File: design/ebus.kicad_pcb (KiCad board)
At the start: 2 copper layers, 64.3 x 65.4 mm, 53 parts, among them J1 EBUS, J2 USB_B_Micro, J3 UART, J4 PROG, J5 PINS, J6 PWR, J7 UART, J8 Measurements, Q1 BC817, U1 LM393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

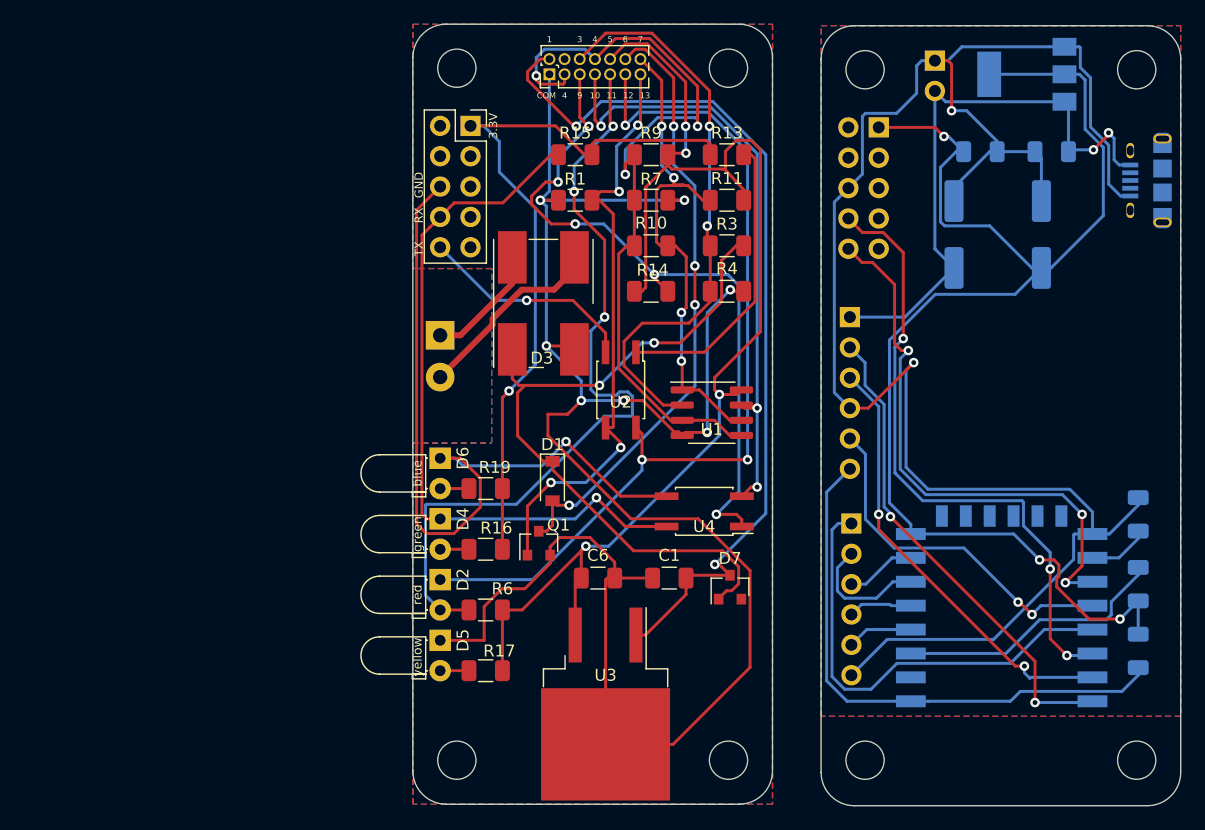
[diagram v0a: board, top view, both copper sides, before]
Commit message: Inverted rx-tx, reposition ebus terminal with measurement points to let attach raspberry with full connector, added programmer to wifi module
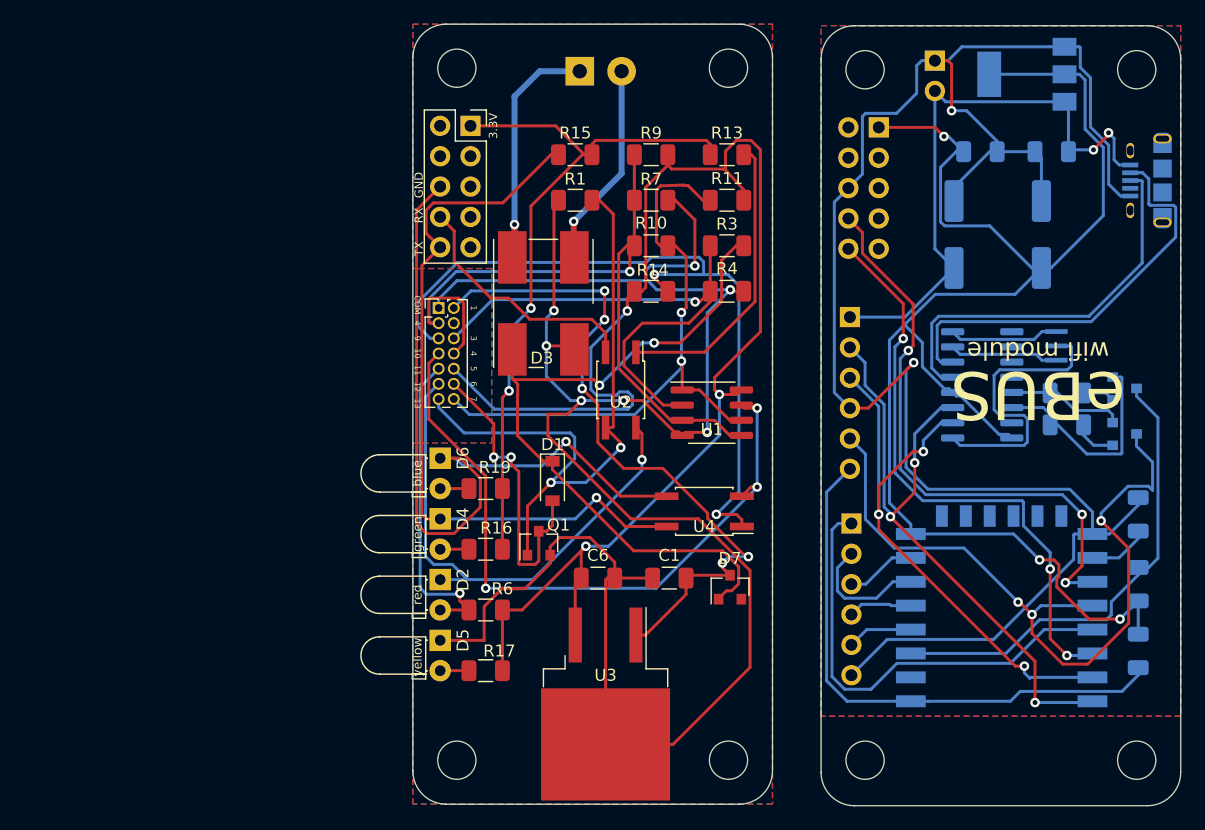
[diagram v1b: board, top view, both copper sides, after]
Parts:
- added Q2: BC817, Package_TO_SOT_SMD:SOT-23, B.Cu at (122.8, 113.5)
- added Q3: BC817, Package_TO_SOT_SMD:SOT-23, B.Cu at (122.8, 117.3)
- added R2: 10k, Resistor_SMD:R_1206_3216Metric, B.Cu at (118.0, 113.9)
- added R5: 10k, Resistor_SMD:R_1206_3216Metric, B.Cu at (118.0, 116.6)
- added U7: CH340G, Package_SO:SOIC-16_3.9x9.9mm_P1.27mm, B.Cu at (110.9, 113.2)
- added Y1: 12MHz 22pF, Crystal:Resonator_SMD_muRata_CSTxExxV-3Pin_3.0x1.1mm, B.Cu at (117.1, 110.0)
- J8: value Measurements -> Conn_02x07_Counter_Clockwise
- moved J1 25.0 mm to (77.2, 87.0), turned to 0 degrees
- moved J8 21.6 mm to (65.4, 106.8), turned to 0 degrees
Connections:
- net Net-(R18-Pad1) renamed EN
- J2 pad 2: (no net) -> Net-(J2-Pad2)
- J2 pad 3: (no net) -> Net-(J2-Pad3)
- J3 pad 10: TX -> RX
- J3 pad 8: RX -> TX
- J7 pad 10: TX -> RX
- J7 pad 8: RX -> TX
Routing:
- net MP11: track 67.1 -> 26.7 mm, vias 3 -> 1
- net Net-(J2-Pad2): track 0.00 -> 35.9 mm
- net Net-(J2-Pad3): track 0.00 -> 33.4 mm
- net GPIO0: track 29.9 -> 62.9 mm, vias 2 -> 3
- net MP12: track 75.4 -> 43.7 mm, vias 3 -> 1
- net MP6: track 51.6 -> 25.9 mm, vias 4 -> 2
- net GNDREF: track 218.0 -> 242.2 mm
- net Net-(Q2-Pad2): track 0.00 -> 18.5 mm
- net MP1: track 75.9 -> 58.7 mm, vias 2 -> 5
- net EN: track 23.0 -> 39.9 mm
- net MP5: track 106.7 -> 121.9 mm, vias 4 -> 3
- net GNDD: track 162.4 -> 175.4 mm
- net P_TX: track 41.0 -> 52.8 mm, vias 2 -> 3
- net P_RX: track 37.1 -> 48.4 mm, vias 2 -> 3
- net +3V3: track 173.7 -> 184.3 mm, vias 4 -> 5
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
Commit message: usbc, updated images
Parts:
- added C7: 22pF, Capacitor_SMD:C_0805_2012Metric, B.Cu at (108.7, 120.3)
- added C8: 22pF, Capacitor_SMD:C_0805_2012Metric, B.Cu at (113.1, 120.3)
- D2, D4, D5, D6: footprint LED_THT:LED_D3.0mm_Horizontal_O1.27mm_Z2.0mm -> Diode_SMD:D_1206_3216Metric
- J2: value USB_B_Micro -> USB_C_Receptacle_USB2.0; footprint usb:AMPHENOL_10118194-0001LF -> Connector_USB:USB_C_Receptacle_HRO_TYPE-C-31-M-12
- R17: value 10k -> 5.1k
- R19: value 10k -> 20k
- Y1: value 12MHz 22pF -> Crystal; footprint Crystal:Resonator_SMD_muRata_CSTxExxV-3Pin_3.0x1.1mm -> Crystal:Crystal_SMD_HC49-SD
- moved J6 19.2 mm to (125.2, 91.8)
- moved U5 17.4 mm to (123.4, 102.3), turned to -90 degrees
- moved J2 14.2 mm to (116.4, 85.6), turned to 0 degrees
- moved R5 6.91 mm to (124.6, 118.5), turned to -90 degrees
- moved R2 6.09 mm to (121.9, 118.5), turned to -90 degrees
- moved J1 5.56 mm to (71.7, 87.0)
- moved Y1 4.97 mm to (117.7, 114.9)
- moved Q2 3.62 mm to (122.5, 109.9)
- moved Q3 3.62 mm to (122.5, 113.7)
- moved D2 1.42 mm to (65.5, 131.0)
- moved D5 1.32 mm to (65.5, 135.9)
- moved D6 1.22 mm to (65.5, 120.6)
- moved D4 1.17 mm to (65.5, 125.6)
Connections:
- J2 pad S1: (no net) -> GNDREF
- J3 pad 2: (no net) -> unconnected-(J3-Pad2)
- J3 pad 3: (no net) -> unconnected-(J3-Pad3)
- J3 pad 4: (no net) -> unconnected-(J3-Pad4)
- J3 pad 5: (no net) -> unconnected-(J3-Pad5)
- J3 pad 7: (no net) -> unconnected-(J3-Pad7)
- J3 pad 9: (no net) -> unconnected-(J3-Pad9)
- J7 pad 2: (no net) -> unconnected-(J7-Pad2)
- J7 pad 3: (no net) -> unconnected-(J7-Pad3)
- J7 pad 4: (no net) -> unconnected-(J7-Pad4)
- J7 pad 5: (no net) -> unconnected-(J7-Pad5)
- J7 pad 7: (no net) -> unconnected-(J7-Pad7)
- J7 pad 9: (no net) -> unconnected-(J7-Pad9)
- J8 pad 4: (no net) -> unconnected-(J8-Pad4)
- U6 pad 10: (no net) -> unconnected-(U6-Pad10)
- U6 pad 11: (no net) -> unconnected-(U6-Pad11)
- U6 pad 12: (no net) -> unconnected-(U6-Pad12)
- U6 pad 13: (no net) -> unconnected-(U6-Pad13)
- U6 pad 14: (no net) -> unconnected-(U6-Pad14)
- U6 pad 2: (no net) -> unconnected-(U6-Pad2)
- U6 pad 9: (no net) -> unconnected-(U6-Pad9)
- U7 pad 10: (no net) -> unconnected-(U7-Pad10)
- U7 pad 11: (no net) -> unconnected-(U7-Pad11)
- U7 pad 12: (no net) -> unconnected-(U7-Pad12)
- U7 pad 15: (no net) -> unconnected-(U7-Pad15)
- U7 pad 5: Net-(J2-Pad3) -> Net-(U7-Pad5)
- U7 pad 6: Net-(J2-Pad2) -> Net-(U7-Pad6)
- U7 pad 8: Net-(U7-Pad8) -> Net-(C8-Pad1)
- U7 pad 9: (no net) -> unconnected-(U7-Pad9)
- Y1 pad 2: GNDREF -> Net-(C8-Pad1)
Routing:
- net Net-(U7-Pad5): track 0.00 -> 39.5 mm, vias 0 -> 2
- net Net-(J2-Pad2): track 35.9 -> 0.00 mm
- net Net-(U7-Pad6): track 0.00 -> 35.6 mm
- net Net-(J2-Pad3): track 33.4 -> 0.00 mm
- net Net-(C7-Pad1): track 9.13 -> 34.1 mm
- net Net-(C8-Pad1): track 0.00 -> 22.3 mm
- net Net-(Q3-Pad2): track 9.86 -> 29.4 mm, vias 0 -> 2
- net +5VP: track 49.5 -> 67.6 mm
- net GNDREF: track 242.2 -> 229.9 mm, vias 3 -> 4
- net Net-(Q2-Pad2): track 18.5 -> 29.1 mm, vias 0 -> 3
- net Net-(U7-Pad8): track 9.21 -> 0.00 mm
- net +3V3: track 184.3 -> 175.6 mm, vias 5 -> 7
- net Net-(Q2-Pad1): track 2.66 -> 7.48 mm
- net EN: track 39.9 -> 44.2 mm
- net Net-(D3-Pad3): track 19.9 -> 15.7 mm
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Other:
- net class Default removed
- net class Power removed
